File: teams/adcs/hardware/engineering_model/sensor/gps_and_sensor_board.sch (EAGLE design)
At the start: 44 parts, among them U1 TPS732XX, U2 TPS732XX, U3 OEM719, U4 LTC3624

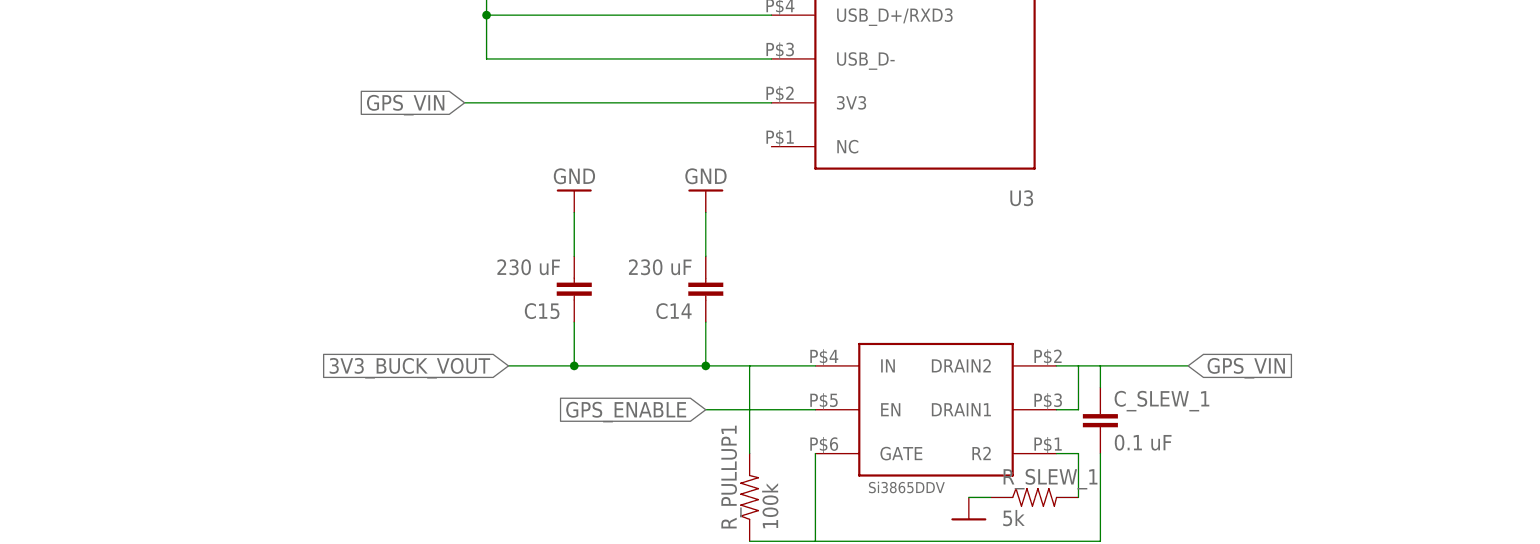
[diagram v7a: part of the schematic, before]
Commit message: ADCS/GPS: Add some smoothing capacitors to GPS switch
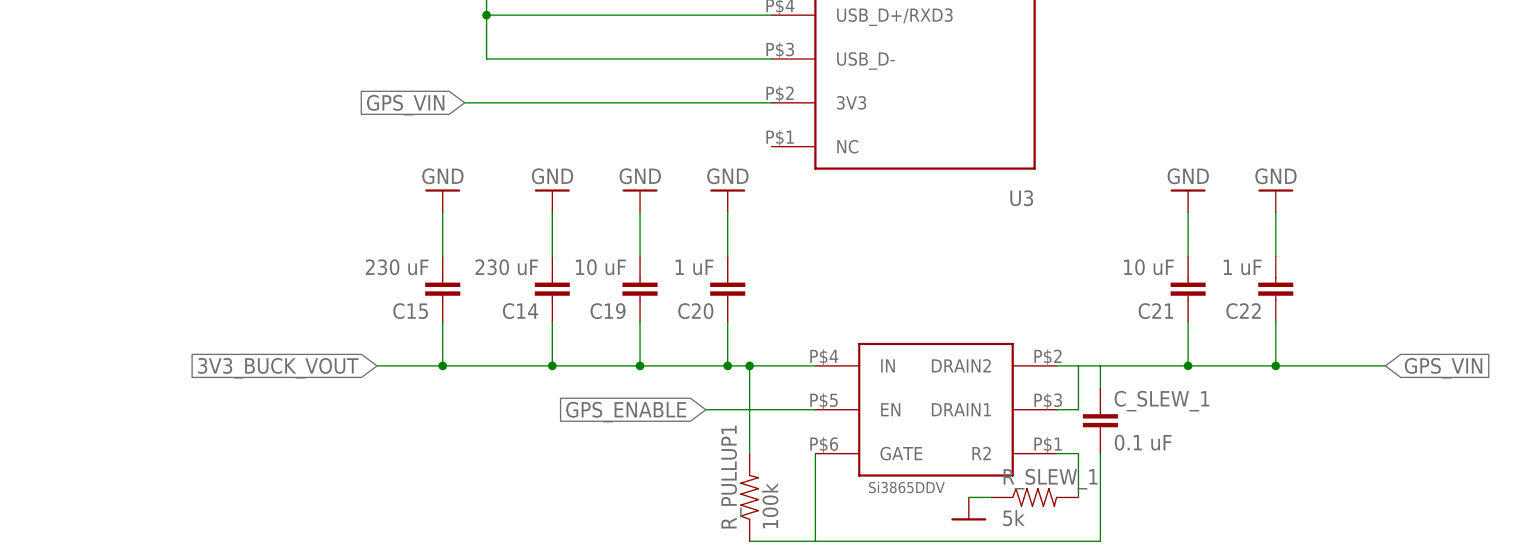
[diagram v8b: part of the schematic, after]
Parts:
- added C19, C21: 10 uF, DubSat1 Components:CAPACITOR0805
- added C20, C22: 1 uF, DubSat1 Components:CAPACITOR0805
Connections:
- net 3V3_BUCK_VOUT: now also C19.1, C20.1
- net GND: now also C19.2, C20.2, C21.2, C22.2
- net GPS_VIN: now also C21.1, C22.1
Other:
- moved on the sheet: C14, C15
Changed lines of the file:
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@@
 <part name="C18" library="DubSat1 Components" deviceset="CAPACITOR" device="0805" value="1 uF"/>
 <part name="GND26" library="supply1" library_urn="urn:adsk.eagle:library:371" deviceset="GND" device=""/>
+<part name="C19" library="DubSat1 Components" deviceset="CAPACITOR" device="0805" value="10 uF"/>
+<part name="GND27" library="supply1" library_urn="urn:adsk.eagle:library:371" deviceset="GND" device=""/>
+<part name="C20" library="DubSat1 Components" deviceset="CAPACITOR" device="0805" value="1 uF"/>
+<part name="GND28" library="supply1" library_urn="urn:adsk.eagle:library:371" deviceset="GND" device=""/>
+<part name="C21" library="DubSat1 Components" deviceset="CAPACITOR" device="0805" value="10 uF"/>
+<part name="GND29" library="supply1" library_urn="urn:adsk.eagle:library:371" deviceset="GND" device=""/>
+<part name="C22" library="DubSat1 Components" deviceset="CAPACITOR" device="0805" value="1 uF"/>
+<part name="GND30" library="supply1" library_urn="urn:adsk.eagle:library:371" deviceset="GND" device=""/>
 </parts>
 <sheets>
@@
 <instance part="GND17" gate="G$1" x="325.12" y="-160.02" smashed="yes"/>
 <instance part="R_PULLUP1" gate="G$1" x="299.72" y="-157.48" rot="R90"/>
-<instance part="C14" gate="G$1" x="294.64" y="-132.08" rot="R180"/>
-<instance part="C15" gate="G$1" x="279.4" y="-132.08" rot="R180"/>
-<instance part="GND18" gate="1" x="279.4" y="-121.92" rot="R180"/>
-<instance part="GND19" gate="1" x="294.64" y="-121.92" rot="R180"/>
+<instance part="C14" gate="G$1" x="276.86" y="-132.08" rot="R180"/>
+<instance part="C15" gate="G$1" x="264.16" y="-132.08" rot="R180"/>
+<instance part="GND18" gate="1" x="264.16" y="-121.92" rot="R180"/>
+<instance part="GND19" gate="1" x="276.86" y="-121.92" rot="R180"/>
 <instance part="C13" gate="G$1" x="330.2" y="50.8"/>
 <instance part="U$2" gate="G$1" x="172.72" y="-139.7"/>
@@
 <instance part="C18" gate="G$1" x="241.3" y="38.1" rot="R180"/>
 <instance part="GND26" gate="1" x="218.44" y="43.18" rot="R270"/>
+<instance part="C19" gate="G$1" x="287.02" y="-132.08" rot="R180"/>
+<instance part="GND27" gate="1" x="287.02" y="-121.92" rot="R180"/>
+<instance part="C20" gate="G$1" x="297.18" y="-132.08" rot="R180"/>
+<instance part="GND28" gate="1" x="297.18" y="-121.92" rot="R180"/>
+<instance part="C21" gate="G$1" x="350.52" y="-132.08" rot="R180"/>
+<instance part="GND29" gate="1" x="350.52" y="-121.92" rot="R180"/>
+<instance part="C22" gate="G$1" x="360.68" y="-132.08" rot="R180"/>
+<instance part="GND30" gate="1" x="360.68" y="-121.92" rot="R180"/>
 </instances>
 <busses>
@@
 <pinref part="GND18" gate="1" pin="GND"/>
 <pinref part="C15" gate="G$1" pin="2"/>
-<wire x1="279.4" y1="-124.46" x2="279.4" y2="-129.54" width="0.1524" layer="91"/>
+<wire x1="264.16" y1="-124.46" x2="264.16" y2="-129.54" width="0.1524" layer="91"/>
 </segment>
 <segment>
 <pinref part="GND19" gate="1" pin="GND"/>
 <pinref part="C14" gate="G$1" pin="2"/>
-<wire x1="294.64" y1="-124.46" x2="294.64" y2="-129.54" width="0.1524" layer="91"/>
+<wire x1="276.86" y1="-124.46" x2="276.86" y2="-129.54" width="0.1524" layer="91"/>
 </segment>
 <segment>
@@
 <wire x1="241.3" y1="43.18" x2="241.3" y2="40.64" width="0.1524" layer="91"/>
 <junction x="231.14" y="43.18"/>
+</segment>
+<segment>
+<pinref part="GND27" gate="1" pin="GND"/>
+<pinref part="C19" gate="G$1" pin="2"/>
+<wire x1="287.02" y1="-124.46" x2="287.02" y2="-129.54" width="0.1524" layer="91"/>
+</segment>
+<segment>
+<pinref part="GND28" gate="1" pin="GND"/>
+<pinref part="C20" gate="G$1" pin="2"/>
+<wire x1="297.18" y1="-124.46" x2="297.18" y2="-129.54" width="0.1524" layer="91"/>
+</segment>
+<segment>
+<pinref part="GND29" gate="1" pin="GND"/>
+<pinref part="C21" gate="G$1" pin="2"/>
+<wire x1="350.52" y1="-124.46" x2="350.52" y2="-129.54" width="0.1524" layer="91"/>
+</segment>
+<segment>
+<pinref part="GND30" gate="1" pin="GND"/>
+<pinref part="C22" gate="G$1" pin="2"/>
+<wire x1="360.68" y1="-124.46" x2="360.68" y2="-129.54" width="0.1524" layer="91"/>
 </segment>
 </net>
@@
 <pinref part="R_PULLUP1" gate="G$1" pin="2"/>
 <wire x1="299.72" y1="-152.4" x2="299.72" y2="-142.24" width="0.1524" layer="91"/>
+<wire x1="299.72" y1="-142.24" x2="297.18" y2="-142.24" width="0.1524" layer="91"/>
+<label x="256.54" y="-142.24" size="1.778" layer="95" rot="R180" xref="yes"/>
+<wire x1="297.18" y1="-142.24" x2="287.02" y2="-142.24" width="0.1524" layer="91"/>
+<wire x1="287.02" y1="-142.24" x2="276.86" y2="-142.24" width="0.1524" layer="91"/>
+<wire x1="276.86" y1="-142.24" x2="264.16" y2="-142.24" width="0.1524" layer="91"/>
+<wire x1="264.16" y1="-142.24" x2="256.54" y2="-142.24" width="0.1524" layer="91"/>
+<pinref part="C15" gate="G$1" pin="1"/>
+<wire x1="264.16" y1="-137.16" x2="264.16" y2="-142.24" width="0.1524" layer="91"/>
+<junction x="264.16" y="-142.24"/>
+<pinref part="C14" gate="G$1" pin="1"/>
+<wire x1="276.86" y1="-137.16" x2="276.86" y2="-142.24" width="0.1524" layer="91"/>
+<junction x="276.86" y="-142.24"/>
 <pinref part="U$3" gate="G$1" pin="IN"/>
 <wire x1="299.72" y1="-142.24" x2="307.34" y2="-142.24" width="0.1524" layer="91"/>
-<wire x1="299.72" y1="-142.24" x2="294.64" y2="-142.24" width="0.1524" layer="91"/>
-<label x="271.78" y="-142.24" size="1.778" layer="95" rot="R180" xref="yes"/>
-<wire x1="294.64" y1="-142.24" x2="279.4" y2="-142.24" width="0.1524" layer="91"/>
-<wire x1="279.4" y1="-142.24" x2="271.78" y2="-142.24" width="0.1524" layer="91"/>
-<pinref part="C15" gate="G$1" pin="1"/>
-<wire x1="279.4" y1="-137.16" x2="279.4" y2="-142.24" width="0.1524" layer="91"/>
-<junction x="279.4" y="-142.24"/>
-<pinref part="C14" gate="G$1" pin="1"/>
-<wire x1="294.64" y1="-137.16" x2="294.64" y2="-142.24" width="0.1524" layer="91"/>
-<junction x="294.64" y="-142.24"/>
+<junction x="299.72" y="-142.24"/>
+<pinref part="C19" gate="G$1" pin="1"/>
+<wire x1="287.02" y1="-137.16" x2="287.02" y2="-142.24" width="0.1524" layer="91"/>
+<junction x="287.02" y="-142.24"/>
+<pinref part="C20" gate="G$1" pin="1"/>
+<wire x1="297.18" y1="-137.16" x2="297.18" y2="-142.24" width="0.1524" layer="91"/>
+<junction x="297.18" y="-142.24"/>
 </segment>
 </net>
@@
 <wire x1="340.36" y1="-144.78" x2="340.36" y2="-142.24" width="0.1524" layer="91"/>
 <wire x1="340.36" y1="-142.24" x2="350.52" y2="-142.24" width="0.1524" layer="91"/>
-<label x="350.52" y="-142.24" size="1.778" layer="95" xref="yes"/>
-</segment>
-</net>
+<label x="373.38" y="-142.24" size="1.778" layer="95" xref="yes"/>
+<pinref part="C21" gate="G$1" pin="1"/>
+<wire x1="350.52" y1="-142.24" x2="360.68" y2="-142.24" width="0.1524" layer="91"/>
+<wire x1="360.68" y1="-142.24" x2="373.38" y2="-142.24" width="0.1524" layer="91"/>
+<wire x1="350.52" y1="-137.16" x2="350.52" y2="-142.24" width="0.1524" layer="91"/>
+<pinref part="C22" gate="G$1" pin="1"/>
+<wire x1="360.68" y1="-137.16" x2="360.68" y2="-142.24" width="0.1524" layer="91"/>
+<junction x="350.52" y="-142.24"/>
+<junction x="360.68" y="-142.24"/>
+</segment>
+</net>
